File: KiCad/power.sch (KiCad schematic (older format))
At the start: 1 part

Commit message: Added Voltage Reg
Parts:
- removed CON?: BARREL_JACK, symbol BARREL_JACK
- added C? (x2): C, symbol C
- added C?: CP, symbol CP
- added R?: R, symbol R
- added U?: LP2989IMX-3.3/NOPBCT, MSOP-8, symbol LP2989IMX-3.3/NOPBCT
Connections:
- net labels added: +3V3, +BATT, ERROR, Earth, SHUTDOWNn
- wire segments 0 -> 11
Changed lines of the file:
@@
 $EndDescr
 $Comp
-L BARREL_JACK CON?
-U 1 1 580FB3AF
-P 1300 1150
-F 0 "CON?" H 1300 1400 50  0000 C CNN
-F 1 "BARREL_JACK" H 1300 950 50  0000 C CNN
-F 2 "" H 1300 1150 50  0000 C CNN
-F 3 "" H 1300 1150 50  0000 C CNN
-	1    1300 1150
+L LP2989IMX-3.3/NOPBCT U?
+U 1 1 5811929F
+P 5150 2750
+F 0 "U?" H 4850 3050 50  0000 C CNN
+F 1 "LP2989IMX-3.3/NOPBCT" H 5350 3050 50  0000 C CNN
+F 2 "MSOP-8" H 5150 2750 50  0000 C CIN
+F 3 "" H 5150 2750 50  0000 C CNN
+	1    5150 2750
 	1    0    0    -1
 $EndComp
+$Comp
+L +BATT #PWR?
+U 1 1 5811986C
+P 4250 2550
+F 0 "#PWR?" H 4250 2400 50  0001 C CNN
+F 1 "+BATT" H 4250 2690 50  0000 C CNN
+F 2 "" H 4250 2550 50  0000 C CNN
+F 3 "" H 4250 2550 50  0000 C CNN
+	1    4250 2550
+	1    0    0    -1
+$EndComp
+$Comp
+L Earth #PWR?
+U 1 1 5811988A
+P 5150 3100
+F 0 "#PWR?" H 5150 2850 50  0001 C CNN
+F 1 "Earth" H 5150 2950 50  0001 C CNN
+F 2 "" H 5150 3100 50  0000 C CNN
+F 3 "" H 5150 3100 50  0000 C CNN
+	1    5150 3100
+	1    0    0    -1
+$EndComp
+$Comp
+L C C?
+U 1 1 581198AC
+P 4650 3000
+F 0 "C?" H 4675 3100 50  0000 L CNN
+F 1 "C" H 4675 2900 50  0000 L CNN
+F 2 "" H 4688 2850 50  0000 C CNN
+F 3 "" H 4650 3000 50  0000 C CNN
+	1    4650 3000
+	1    0    0    -1
+$EndComp
+$Comp
+L Earth #PWR?
+U 1 1 581198DA
+P 4650 3150
+F 0 "#PWR?" H 4650 2900 50  0001 C CNN
+F 1 "Earth" H 4650 3000 50  0001 C CNN
+F 2 "" H 4650 3150 50  0000 C CNN
+F 3 "" H 4650 3150 50  0000 C CNN
+	1    4650 3150
+	1    0    0    -1
+$EndComp
+$Comp
+L +3V3 #PWR?
+U 1 1 581198FA
+P 6050 2700
+F 0 "#PWR?" H 6050 2550 50  0001 C CNN
+F 1 "+3V3" H 6050 2840 50  0000 C CNN
+F 2 "" H 6050 2700 50  0000 C CNN
+F 3 "" H 6050 2700 50  0000 C CNN
+	1    6050 2700
+	1    0    0    -1
+$EndComp
+Wire Wire Line
+	5650 2700 6050 2700
+Wire Wire Line
+	5650 2550 5700 2550
+Wire Wire Line
+	5700 2550 5700 2700
+Connection ~ 5700 2700
+$Comp
+L R R?
+U 1 1 581199B0
+P 5850 2850
+F 0 "R?" V 5930 2850 50  0000 C CNN
+F 1 "R" V 5850 2850 50  0000 C CNN
+F 2 "" V 5780 2850 50  0000 C CNN
+F 3 "" H 5850 2850 50  0000 C CNN
+	1    5850 2850
+	1    0    0    -1
+$EndComp
+Wire Wire Line
+	5650 2950 5700 2950
+Wire Wire Line
+	5700 2950 5700 3000
+Wire Wire Line
+	5700 3000 6250 3000
+Text GLabel 6250 3000 2    60   Output ~ 0
+ERROR
+Connection ~ 5850 3000
+$Comp
+L CP C?
+U 1 1 58119A57
+P 6400 2450
+F 0 "C?" H 6425 2550 50  0000 L CNN
+F 1 "CP" H 6425 2350 50  0000 L CNN
+F 2 "" H 6438 2300 50  0000 C CNN
+F 3 "" H 6400 2450 50  0000 C CNN
+	1    6400 2450
+	1    0    0    -1
+$EndComp
+$Comp
+L Earth #PWR?
+U 1 1 58119B2A
+P 6400 2600
+F 0 "#PWR?" H 6400 2350 50  0001 C CNN
+F 1 "Earth" H 6400 2450 50  0001 C CNN
+F 2 "" H 6400 2600 50  0000 C CNN
+F 3 "" H 6400 2600 50  0000 C CNN
+	1    6400 2600
+	1    0    0    -1
+$EndComp
+Wire Wire Line
+	6400 2300 5850 2300
+Wire Wire Line
+	5850 2300 5850 2700
+Connection ~ 5850 2700
+Text GLabel 4650 2750 0    60   Input ~ 0
+SHUTDOWNn
+$Comp
+L C C?
+U 1 1 58119EFE
+P 4750 2100
+F 0 "C?" H 4775 2200 50  0000 L CNN
+F 1 "C" H 4775 2000 50  0000 L CNN
+F 2 "" H 4788 1950 50  0000 C CNN
+F 3 "" H 4750 2100 50  0000 C CNN
+	1    4750 2100
+	1    0    0    -1
+$EndComp
+$Comp
+L Earth #PWR?
+U 1 1 58119F96
+P 4750 2250
+F 0 "#PWR?" H 4750 2000 50  0001 C CNN
+F 1 "Earth" H 4750 2100 50  0001 C CNN
+F 2 "" H 4750 2250 50  0000 C CNN
+F 3 "" H 4750 2250 50  0000 C CNN
+	1    4750 2250
+	1    0    0    -1
+$EndComp
+Wire Wire Line
+	4650 2550 4250 2550
+Wire Wire Line
+	4750 1950 4450 1950
+Wire Wire Line
+	4450 1950 4450 2550
+Connection ~ 4450 2550
 $EndSCHEMATC

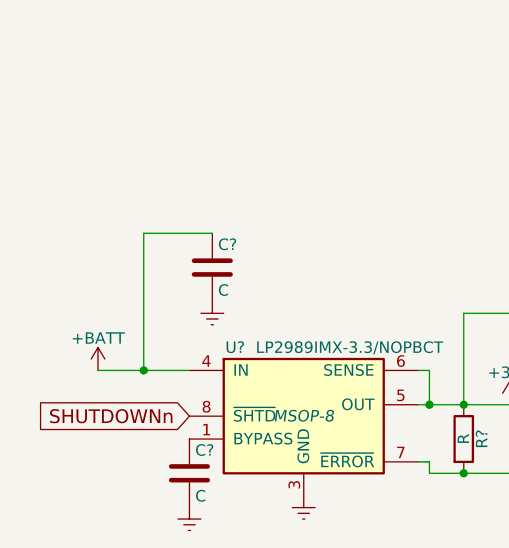
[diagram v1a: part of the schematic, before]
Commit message: Added battery connector
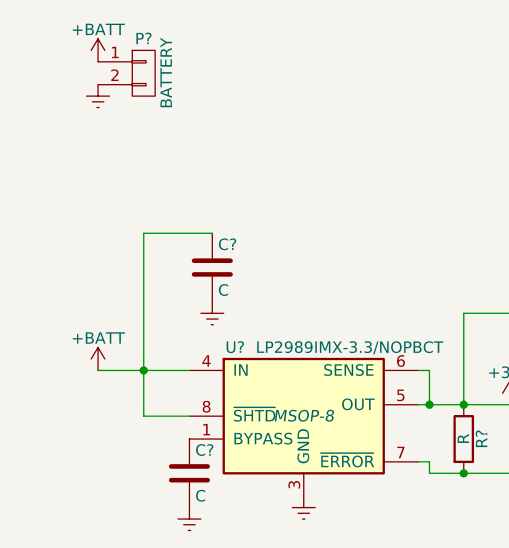
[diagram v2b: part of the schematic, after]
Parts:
- added P?: BATTERY, symbol CONN_01X02
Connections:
- net SHUTDOWNn is gone; now on net +BATT: U?.8 (~SHTD)
- net +BATT: now also P?.1 (P1)
- net Earth: now also P?.2 (P2)
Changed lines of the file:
@@
 	5850 2300 5850 2700
 Connection ~ 5850 2700
-Text GLabel 4650 2750 0    60   Input ~ 0
-SHUTDOWNn
 $Comp
 L C C?
@@
 	4750 1950 4450 1950
 Wire Wire Line
-	4450 1950 4450 2550
+	4450 1950 4450 2750
 Connection ~ 4450 2550
+$Comp
+L CONN_01X02 P?
+U 1 1 5811A8FB
+P 4450 1250
+F 0 "P?" H 4450 1400 50  0000 C CNN
+F 1 "BATTERY" V 4550 1250 50  0000 C CNN
+F 2 "" H 4450 1250 50  0000 C CNN
+F 3 "" H 4450 1250 50  0000 C CNN
+	1    4450 1250
+	1    0    0    -1
+$EndComp
+$Comp
+L Earth #PWR?
+U 1 1 5811A94F
+P 4250 1300
+F 0 "#PWR?" H 4250 1050 50  0001 C CNN
+F 1 "Earth" H 4250 1150 50  0001 C CNN
+F 2 "" H 4250 1300 50  0000 C CNN
+F 3 "" H 4250 1300 50  0000 C CNN
+	1    4250 1300
+	1    0    0    -1
+$EndComp
+$Comp
+L +BATT #PWR?
+U 1 1 5811A975
+P 4250 1200
+F 0 "#PWR?" H 4250 1050 50  0001 C CNN
+F 1 "+BATT" H 4250 1340 50  0000 C CNN
+F 2 "" H 4250 1200 50  0000 C CNN
+F 3 "" H 4250 1200 50  0000 C CNN
+	1    4250 1200
+	1    0    0    -1
+$EndComp
+Wire Wire Line
+	4450 2750 4650 2750
 $EndSCHEMATC
